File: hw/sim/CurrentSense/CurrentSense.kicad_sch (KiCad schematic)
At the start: 23 parts, among them U1 OPAMP

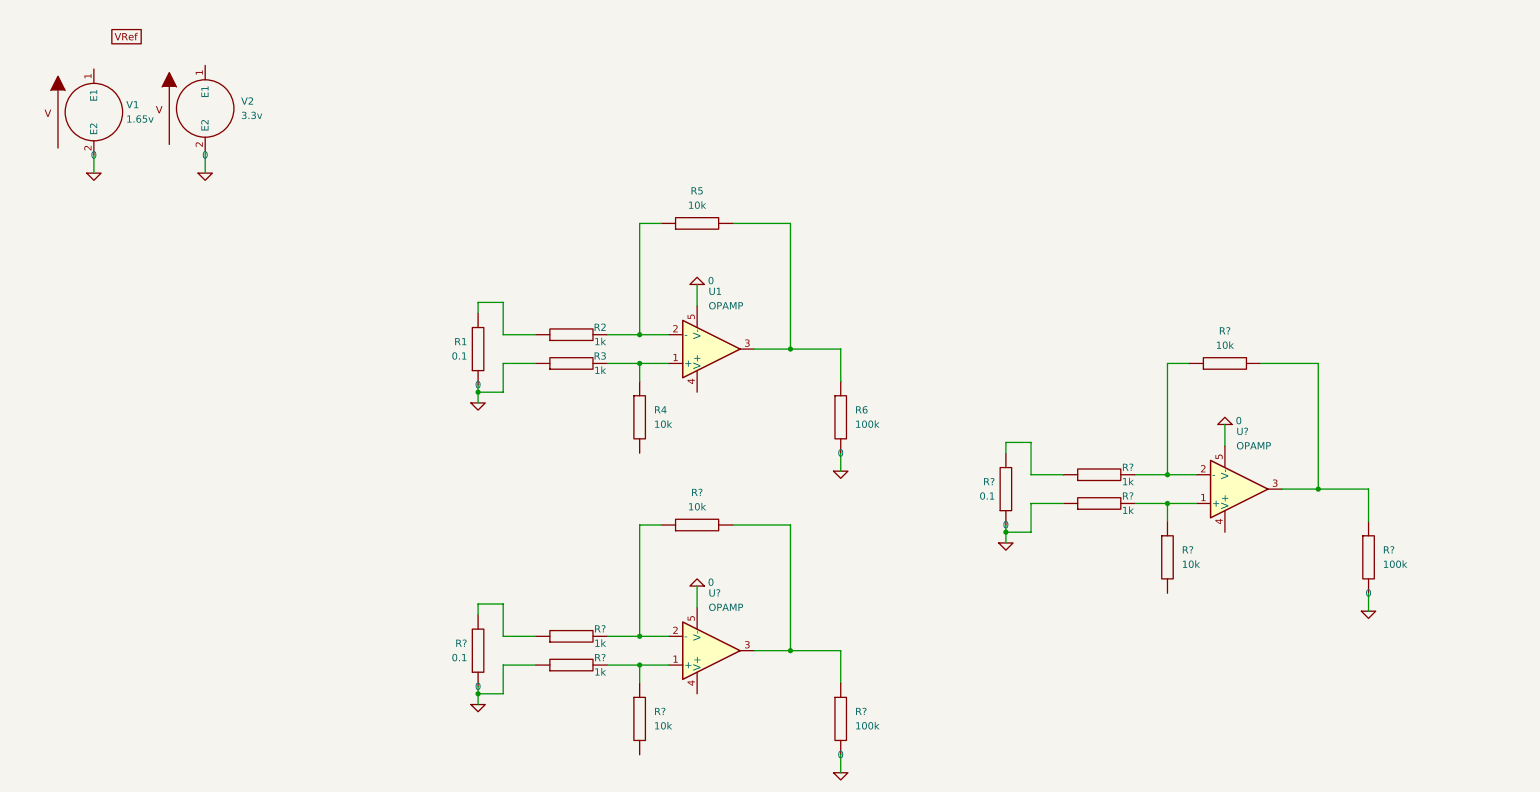
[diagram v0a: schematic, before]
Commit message: Update a few issues with the analog and power stage
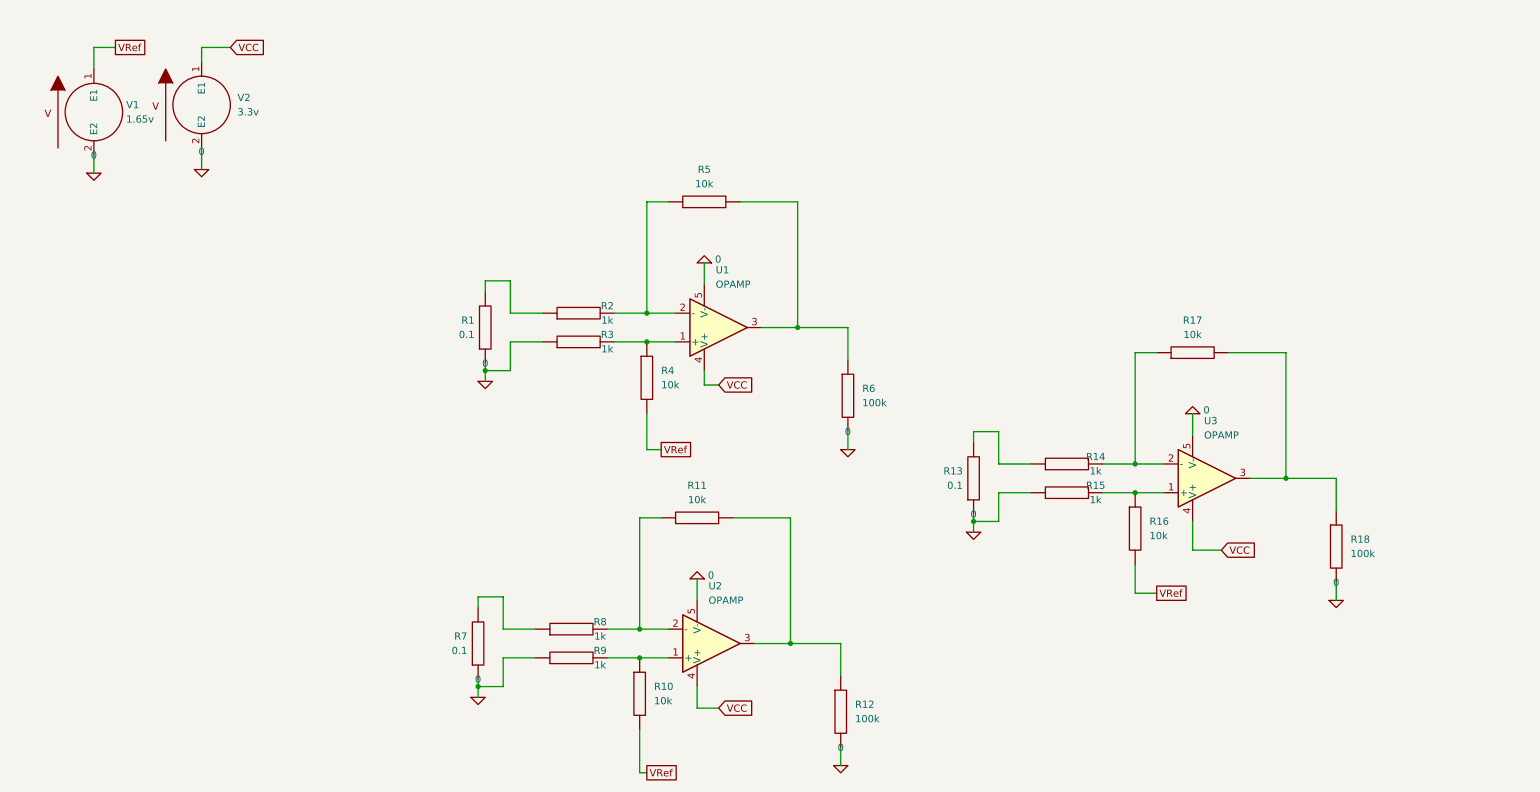
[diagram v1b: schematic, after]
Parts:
- gave numbers to parts that had none: 14
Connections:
- net VRef: now also R10.2, R16.2, R4.2, V1.1 (E1)
- net VCC: now reaches U2.4 (V+)
- net VCC: now also U1.4 (V+), U3.4 (V+), V2.1 (E1)
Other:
- moved on the sheet: R1, R10, R11, R12, R13, R14, R15, R16, R17, R18, R2, R3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

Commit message: Sync PCB updates
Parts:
- added C1, C2, C3, C4, C5, C6: C, symbol pspice:C
- added R19, R20: 100k, symbol pspice:R
- added R21, R22, R23: R, symbol pspice:R
- added U4: OPAMP, symbol pspice:OPAMP
- V1: value 1.65v -> 3.3V; Spice_Model (none) -> trrandom(1 1m 0 10m 3.3); Spice_Netlist_Enabled (none) -> Y; Spice_Primitive (none) -> V
- V2: Spice_Model dc 3.3 -> trrandom(1 0.001 0 0.05 3.3)
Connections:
- net 0: now also C1.2, C2.2, C4.2, C5.2, C6.2, R20.1, U4.5 (V-)
- net VCC: now also C5.1, C6.1, R23.2, U4.4 (V+); no longer V2.1 (E1)
- net VRef: now also C4.1, R21.2, R22.2; no longer V1.1 (E1)
- new net: C2.1, R19.1, R20.2, U4.1 (+)
- new net: C3.2, R22.1, U4.3
- new net: C3.1, R21.1, U4.2 (-)
- new net: R23.1, V2.1 (E1)
- new net VCC_Noisy: C1.1, R19.2, V1.1 (E1)

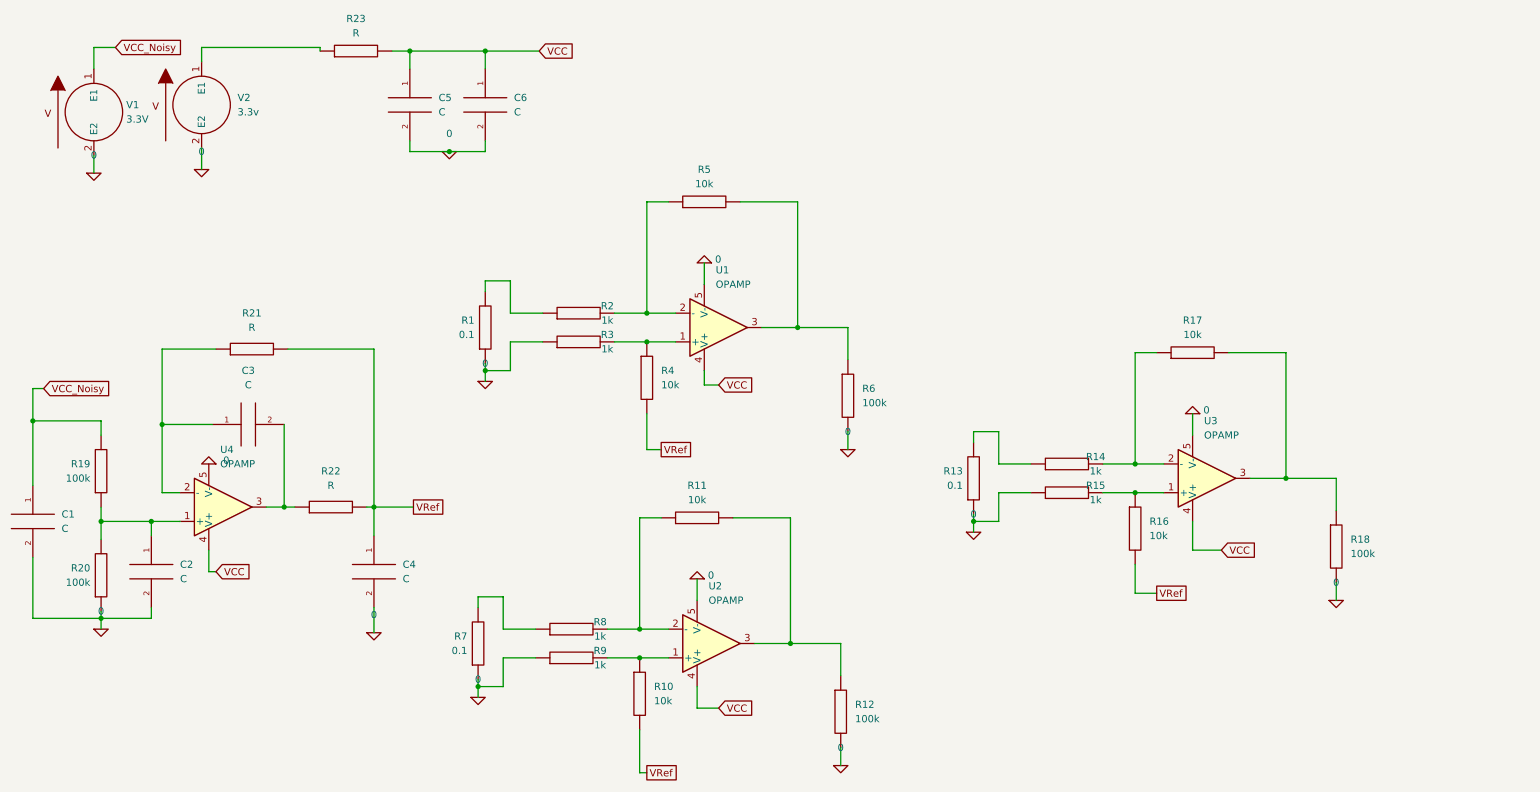
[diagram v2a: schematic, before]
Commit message: Update PCB to fix comparator pin swap
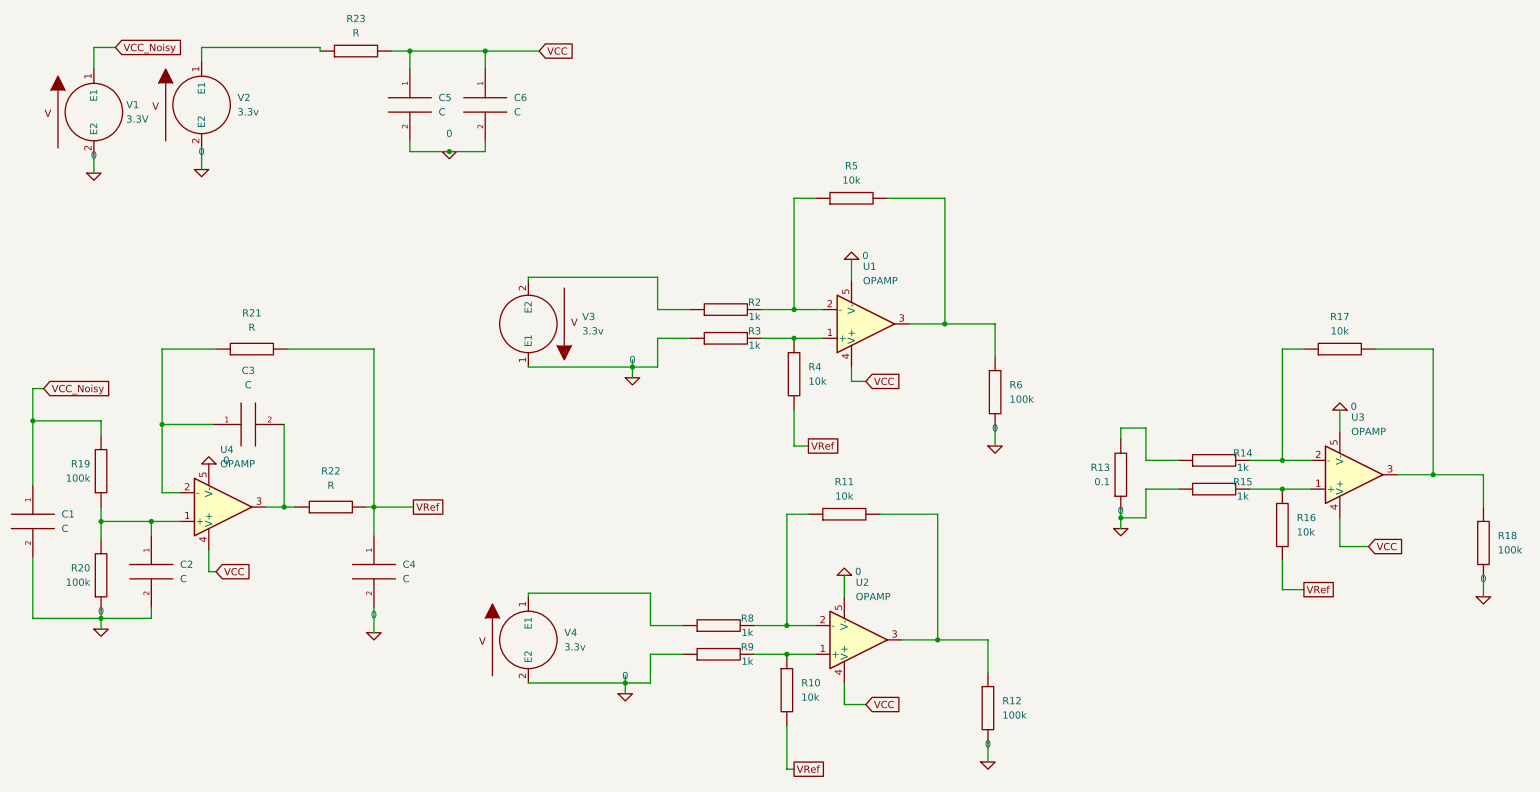
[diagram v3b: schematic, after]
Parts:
- removed R1, R7: 0.1, symbol pspice:R
- added V3, V4: 3.3v, symbol pspice:VSOURCE
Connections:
- net 0: now also V3.1 (E1), V4.2 (E2)
- net at R2.1: now also V3.2 (E2)
- net at R8.1: now also V4.1 (E1)
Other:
- moved on the sheet: R10, R11, R12, R13, R14, R15, R16, R17, R18, R2, R3, R4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

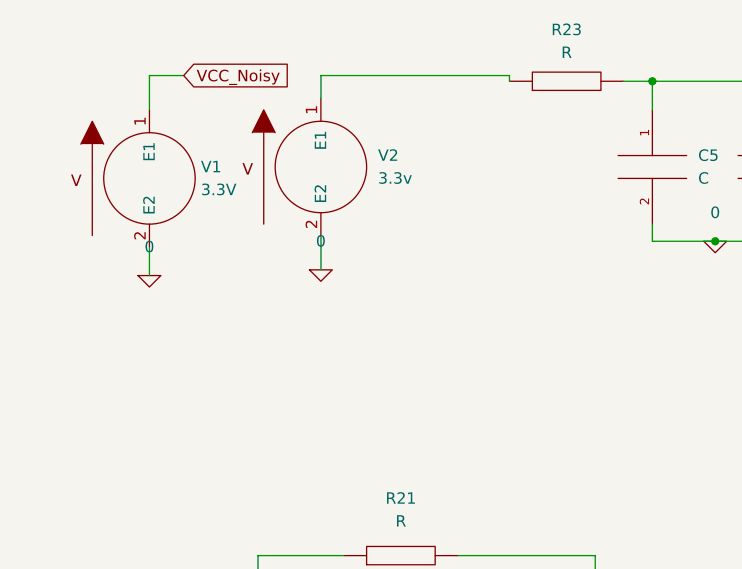
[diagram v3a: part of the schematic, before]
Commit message: Try and figure out current sense issues
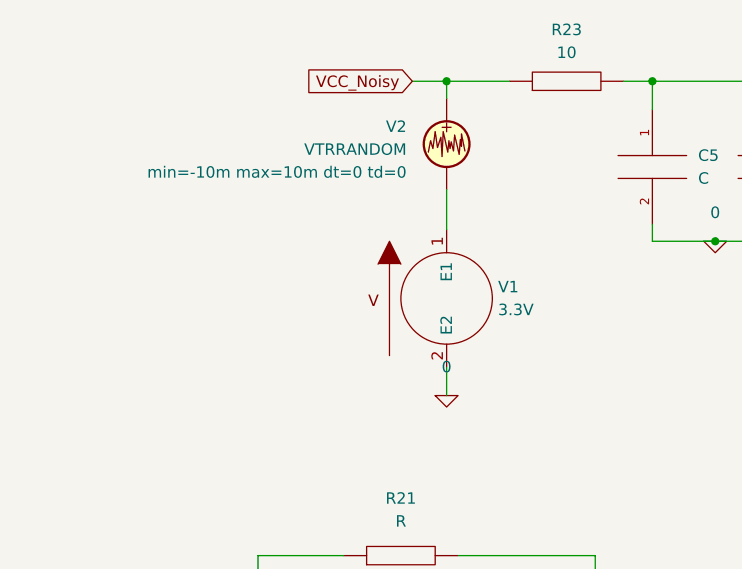
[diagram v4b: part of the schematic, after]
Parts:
- removed V2: 3.3v, symbol pspice:VSOURCE
- added V2: VTRRANDOM, symbol Simulation_SPICE:VTRRANDOM
- C1, C6: Spice_Model 100nF -> (none); Spice_Netlist_Enabled Y -> (none); Spice_Primitive C -> (none)
- C2, C5: Spice_Model 2.2uF -> (none); Spice_Netlist_Enabled Y -> (none); Spice_Primitive C -> (none)
- C3: Spice_Model 33nF -> (none); Spice_Netlist_Enabled Y -> (none); Spice_Primitive C -> (none)
- C4: Spice_Model 1uF -> (none); Spice_Netlist_Enabled Y -> (none); Spice_Primitive C -> (none)
- R10, R16, R4: Spice_Model 10k -> (none); Spice_Netlist_Enabled Y -> (none); Spice_Primitive R -> (none)
- R12, R18, R19, R20, R6: Spice_Model 100k -> (none); Spice_Netlist_Enabled Y -> (none); Spice_Primitive R -> (none)
- R21: Spice_Model 2k -> (none); Spice_Netlist_Enabled Y -> (none); Spice_Primitive R -> (none)
- R22: Spice_Model 33 -> (none); Spice_Netlist_Enabled Y -> (none); Spice_Primitive R -> (none)
- R23: value R -> 10
- U1, U2, U3, U4: Spice_Lib_File uopamp_v1.1.lib -> (none); Spice_Model uopamp_lvl2 -> (none); Spice_Netlist_Enabled Y -> (none); Spice_Node_Sequence 1 2 4 5 3 -> (none); Spice_Primitive X -> (none)
- V1: Spice_Model trrandom(1 1m 0 10m 3.3) -> (none); Spice_Netlist_Enabled Y -> (none); Spice_Primitive V -> (none)
- V3: Spice_Model pulse(0 10m 500m 250u 250u 1 1) -> (none); Spice_Netlist_Enabled Y -> (none); Spice_Primitive V -> (none)
- V4: Spice_Model pulse(0 5m 600m 250u 250u 1 1) -> (none); Spice_Netlist_Enabled Y -> (none); Spice_Primitive V -> (none)
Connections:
- net VCC_Noisy: now also R23.1, V2.1; no longer V1.1 (E1)
- new net: V1.1 (E1), V2.2
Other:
- moved on the sheet: V1
